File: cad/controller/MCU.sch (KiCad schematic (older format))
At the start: 37 parts, among them J3 Conn_02x03_Odd_Even, J4 Conn_01x02, J5 Conn_01x04, J6 Conn_01x05, J7 6P6C, SW2 SW_Push, U5 ATmega328-PU, U6 PCA9517A, U7 TXB0104D, Y2 18MHz

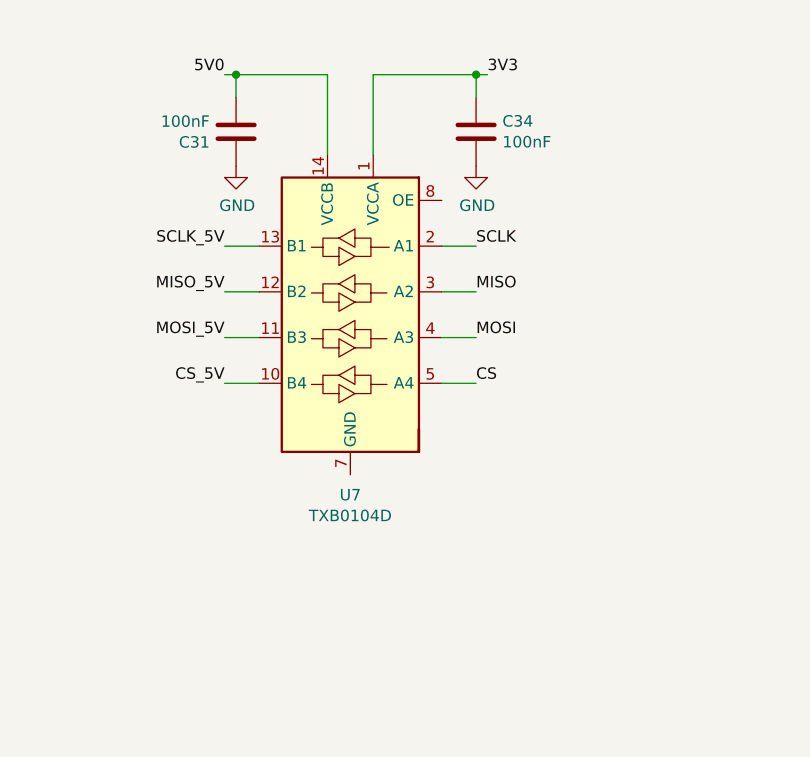
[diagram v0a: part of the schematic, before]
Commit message: Finished placement of controller
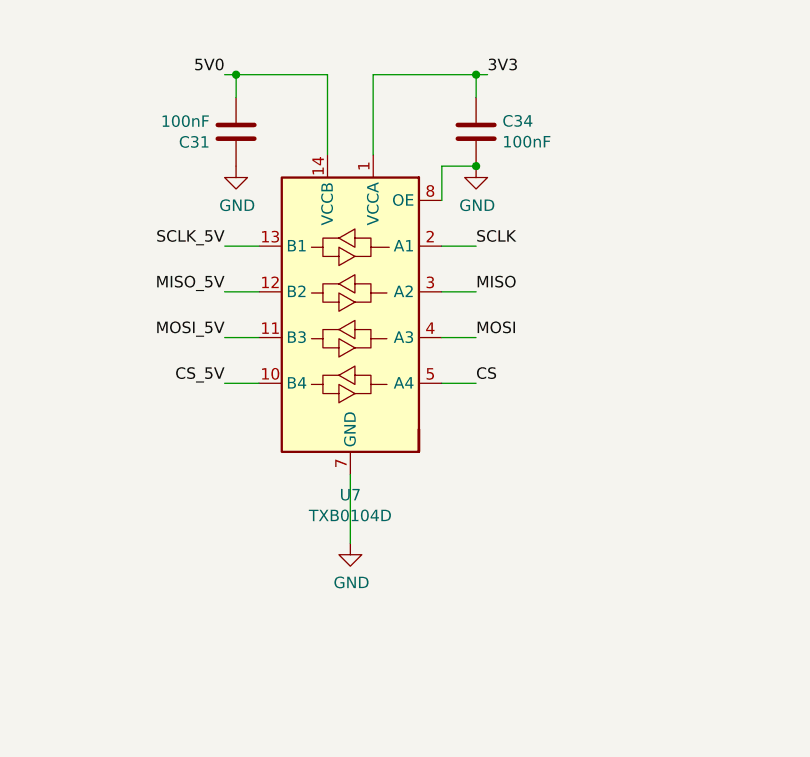
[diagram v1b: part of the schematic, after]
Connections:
- net GND: now also U7.7 (GND), U7.8 (OE)
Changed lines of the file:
@@
 Wire Wire Line
 	4950 3400 5100 3400
+Wire Wire Line
+	6650 5650 6650 5950
+Wire Wire Line
+	7050 4450 7050 4300
+Wire Wire Line
+	7050 4300 7200 4300
+Connection ~ 7200 4300
+$Comp
+L power:GND #PWR?
+U 1 1 62DBDB96
+P 6650 5950
+F 0 "#PWR?" H 6650 5700 50  0001 C CNN
+F 1 "GND" H 6655 5777 50  0000 C CNN
+F 2 "" H 6650 5950 50  0001 C CNN
+F 3 "" H 6650 5950 50  0001 C CNN
+	1    6650 5950
+	1    0    0    -1
+$EndComp
 $EndSCHEMATC

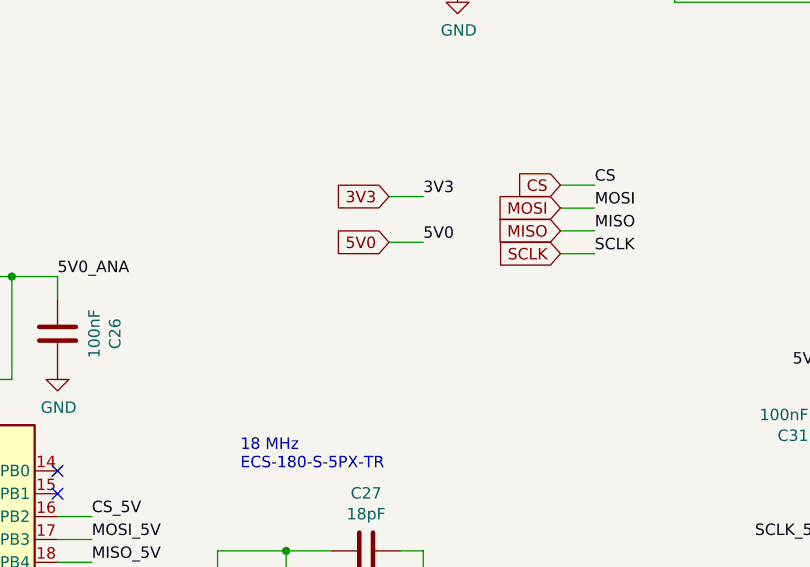
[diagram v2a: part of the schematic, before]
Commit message: Continued controller routing
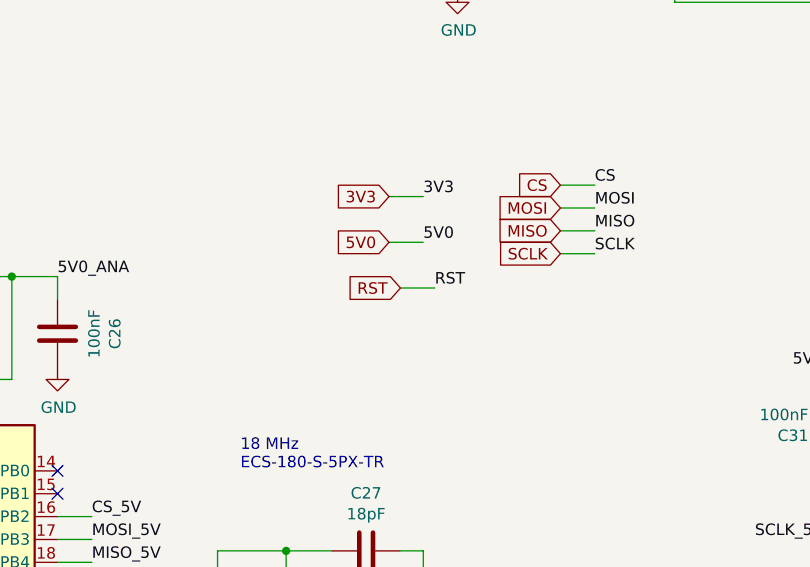
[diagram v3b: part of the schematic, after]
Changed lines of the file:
@@
 	1    0    0    -1
 $EndComp
+Text Label 4400 3550 0    50   ~ 0
+RST
+Text GLabel 4250 3550 0    50   Input ~ 0
+RST
+Wire Wire Line
+	4250 3550 4400 3550
 $EndSCHEMATC

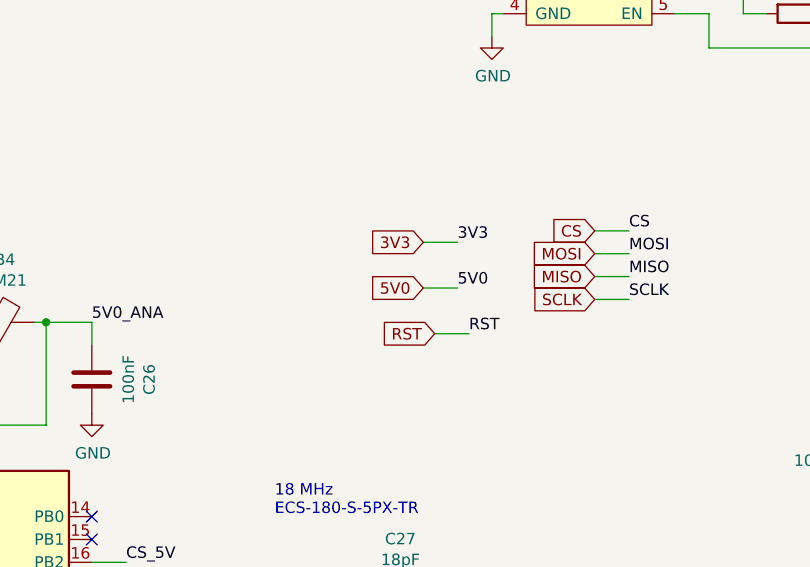
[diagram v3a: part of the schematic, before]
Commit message: Continued routing controller board
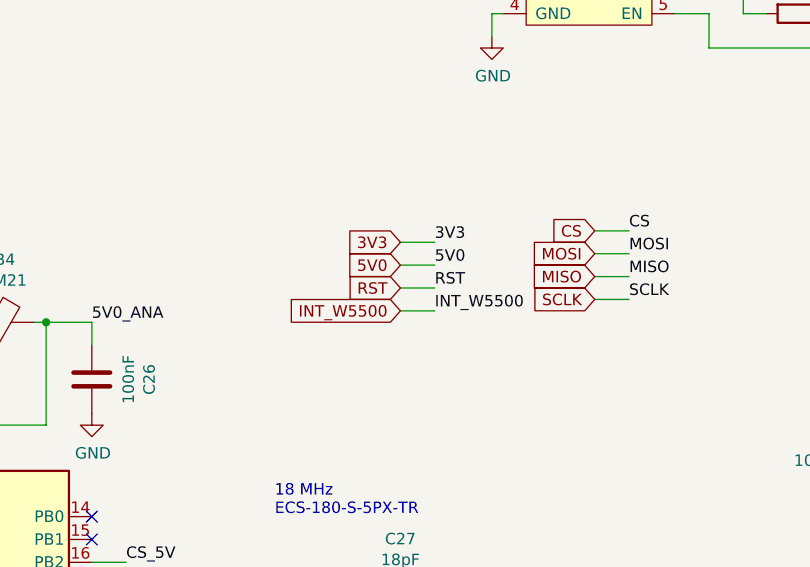
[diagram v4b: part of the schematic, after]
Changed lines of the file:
@@
 Text Notes 7100 2500 0    50   ~ 0
 150 Ohm and 150 pF\ntypical damping values,\nif required
-Text GLabel 4200 3150 0    50   Input ~ 0
+Text GLabel 4100 3150 0    50   Input ~ 0
 3V3
-Text Label 4350 3150 0    50   ~ 0
+Text Label 4250 3150 0    50   ~ 0
 3V3
 Wire Wire Line
-	4200 3150 4350 3150
-Text GLabel 4200 3350 0    50   Input ~ 0
+	4100 3150 4250 3150
+Text GLabel 4100 3250 0    50   Input ~ 0
 5V0
-Text Label 4350 3350 0    50   ~ 0
+Text Label 4250 3250 0    50   ~ 0
 5V0
 Wire Wire Line
-	4200 3350 4350 3350
+	4100 3250 4250 3250
 Text Label 5100 3400 0    50   ~ 0
 SCLK
@@
 	1    0    0    -1
 $EndComp
-Text Label 4400 3550 0    50   ~ 0
+Text Label 4250 3350 0    50   ~ 0
 RST
-Text GLabel 4250 3550 0    50   Input ~ 0
+Text GLabel 4100 3350 0    50   Input ~ 0
 RST
 Wire Wire Line
-	4250 3550 4400 3550
+	4100 3350 4250 3350
+Text Label 4250 3450 0    50   ~ 0
+INT_W5500
+Text GLabel 4100 3450 0    50   Input ~ 0
+INT_W5500
+Wire Wire Line
+	4100 3450 4250 3450
 $EndSCHEMATC

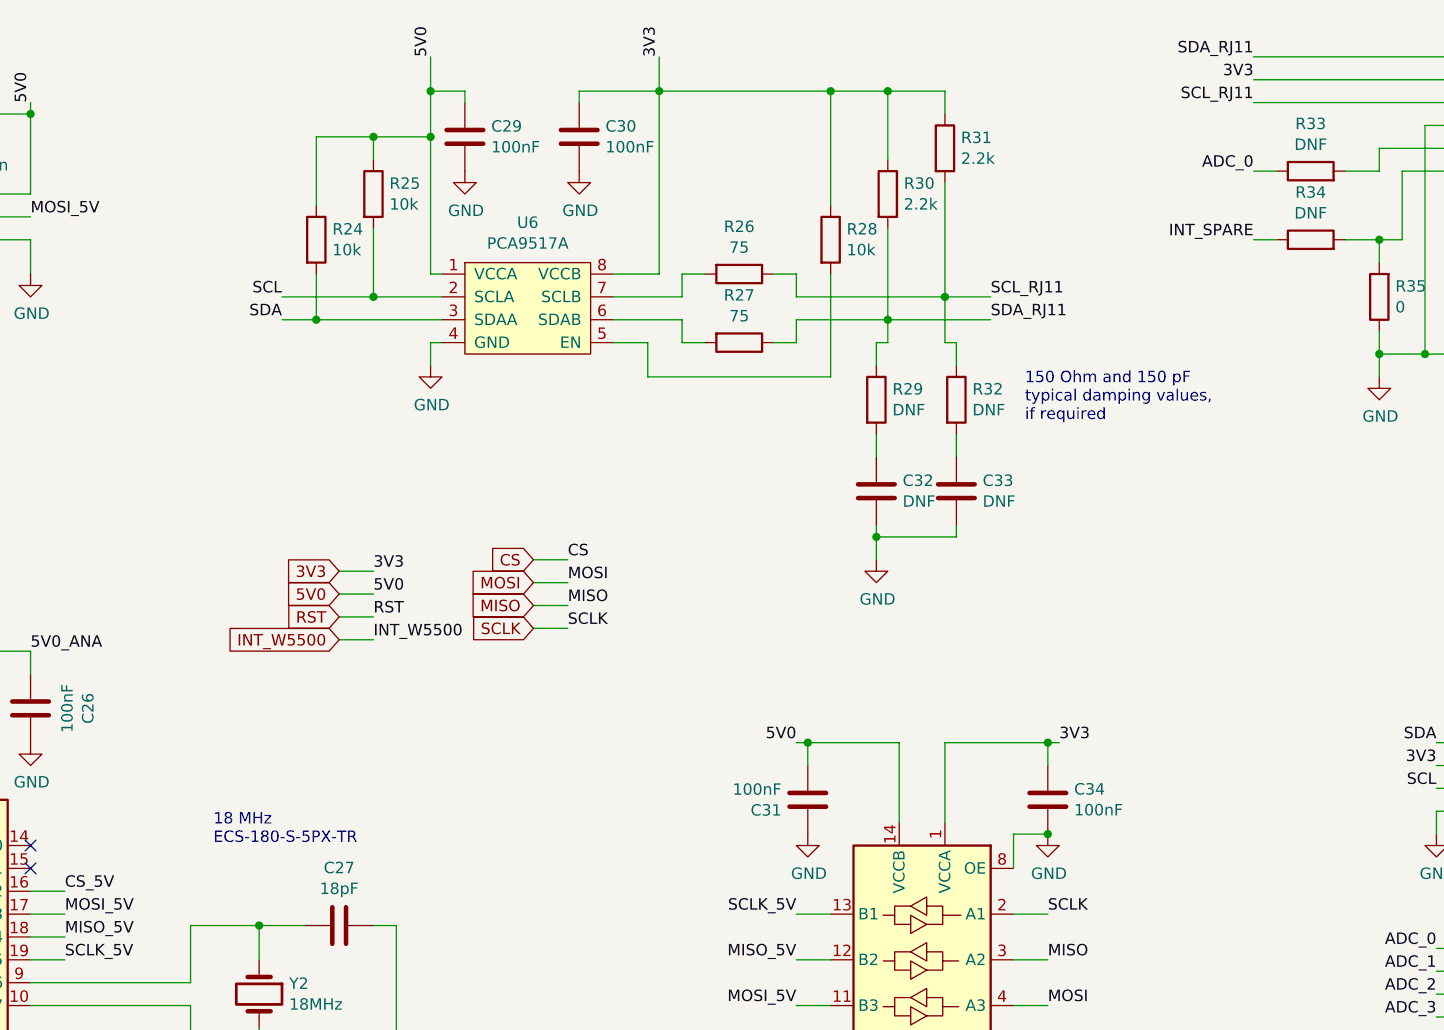
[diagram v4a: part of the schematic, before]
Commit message: Finished PCB layout
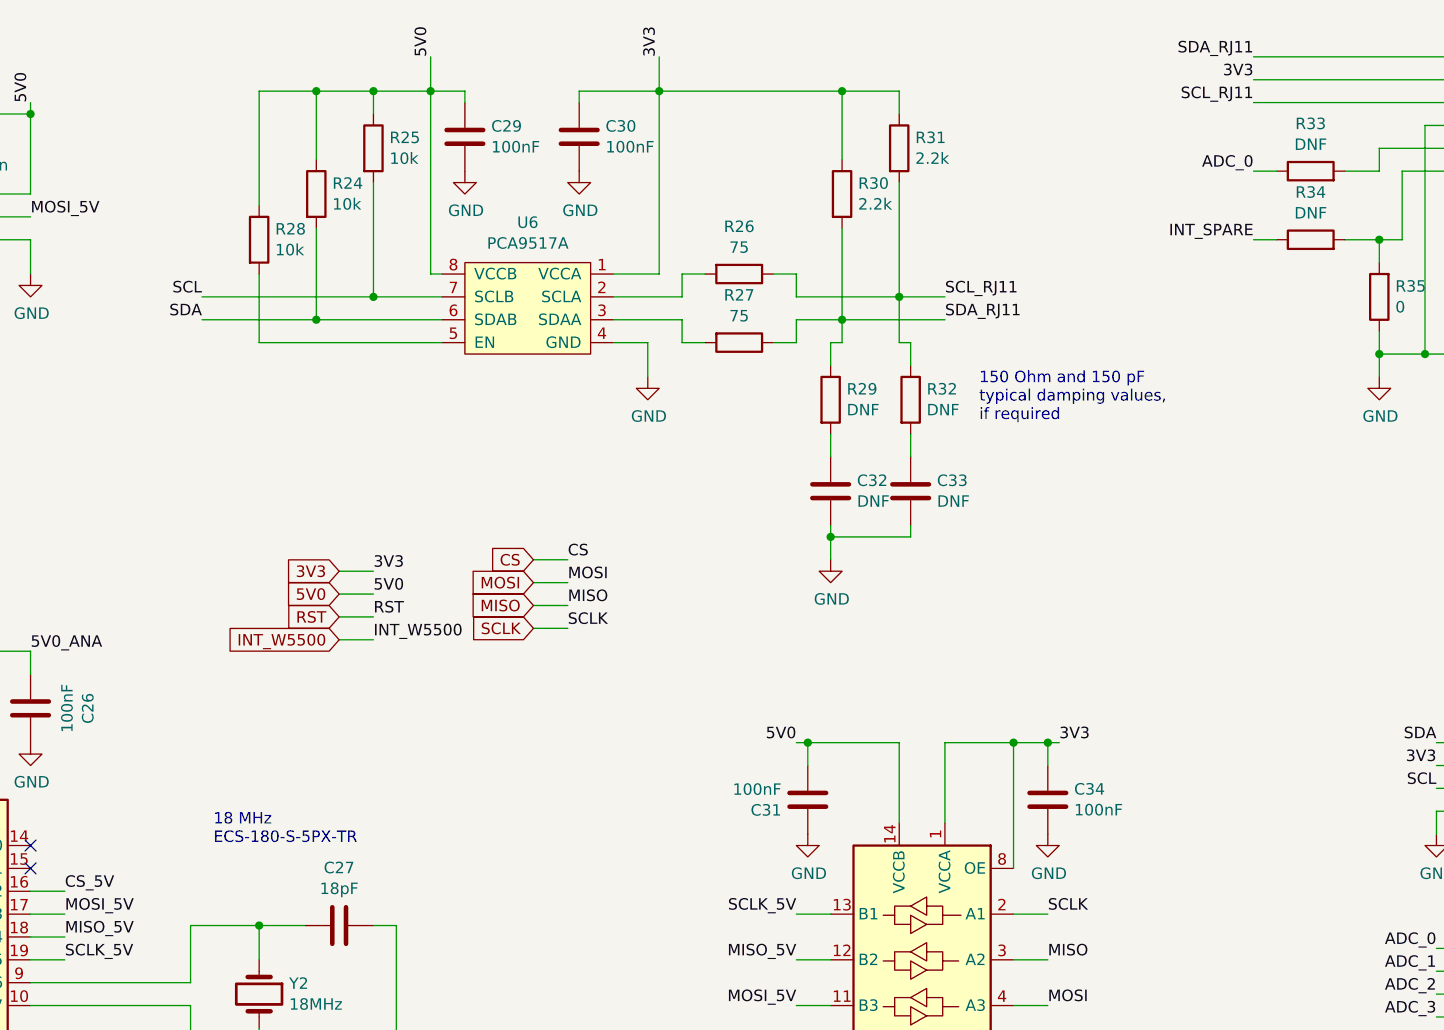
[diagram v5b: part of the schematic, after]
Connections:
- net 3V3: now also U6.1 (VCCA), U7.8 (OE); no longer R28.1, U6.8 (VCCB)
- net 5V0: now also R28.1, U6.8 (VCCB); no longer U6.1 (VCCA)
- net GND: no longer U7.8 (OE)
- net SCL: now also U6.7 (SCLB); no longer U6.2 (SCLA)
- net SDA: now also U6.6 (SDAB); no longer U6.3 (SDAA)
- net at R27.2: now also U6.3 (SDAA); no longer U6.6 (SDAB)
- net at R26.2: now also U6.2 (SCLA); no longer U6.7 (SCLB)
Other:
- moved on the sheet: C32, C33, R24, R25, R28, R29, R30, R31, R32
